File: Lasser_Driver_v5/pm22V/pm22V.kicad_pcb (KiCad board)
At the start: 2 copper layers, 160 x 100 mm, 26 parts, among them J5 Screw_Terminal_01x03, J6 DIN41612_M_3x8+8_Power_Male, Q1 IRF540NPBF, Q2 IRF9540NPBF

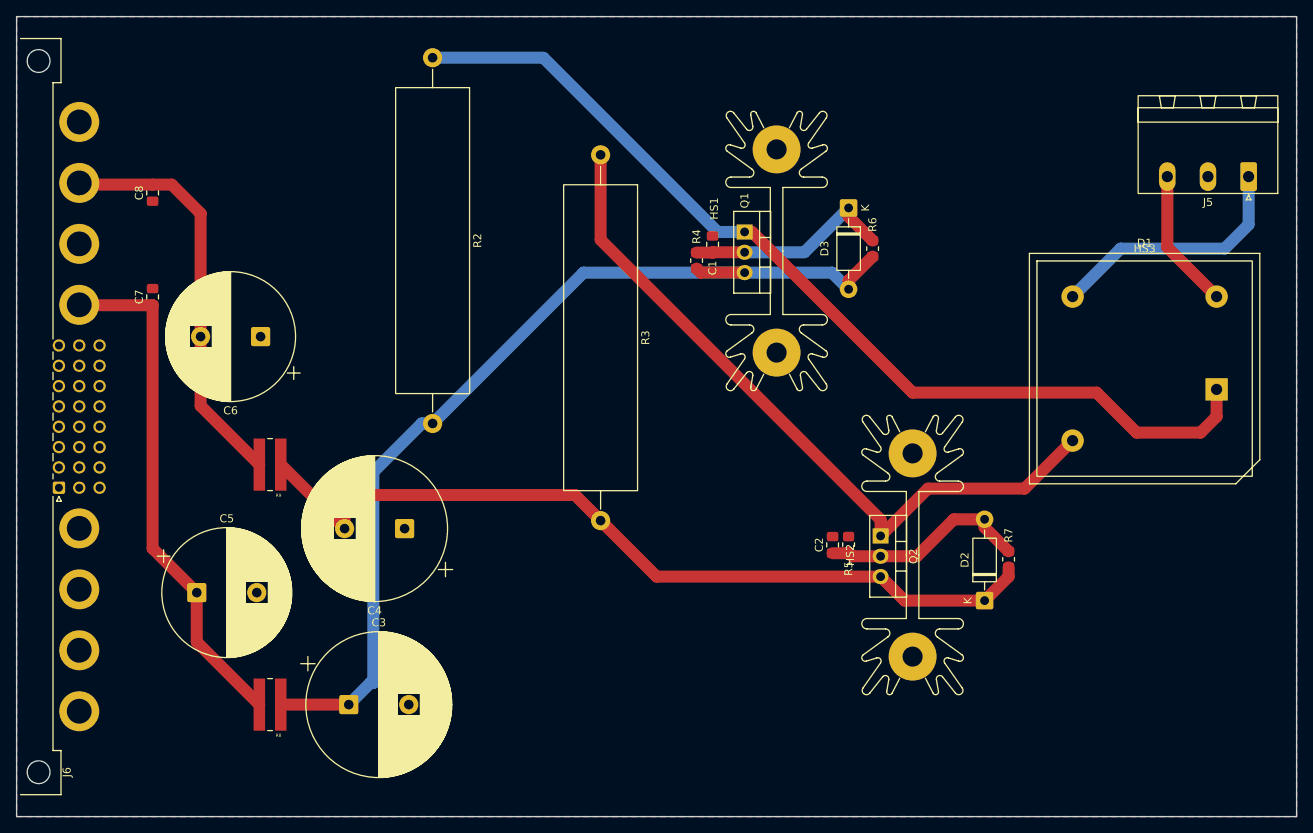
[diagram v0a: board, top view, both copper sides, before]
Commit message: v5 ac board and pm22V board ready
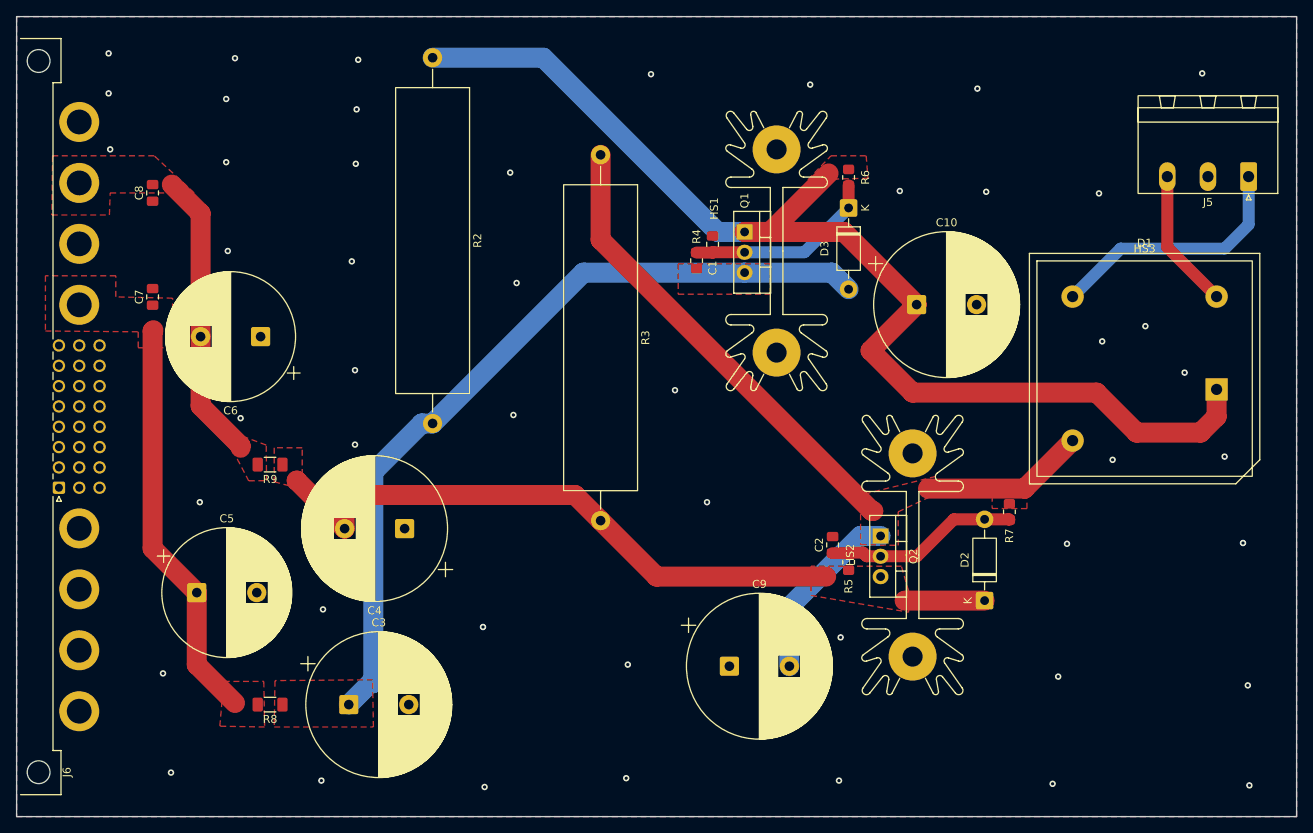
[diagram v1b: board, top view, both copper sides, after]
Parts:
- added C10: 2200uF 50V, Capacitor_THT:CP_Radial_D18.0mm_P7.50mm, F.Cu at (167.5, 81.0)
- added C9: 2200uF 50V, Capacitor_THT:CP_Radial_D18.0mm_P7.50mm, F.Cu at (144.1, 126.2)
- R8: value 4.75 2W -> 0.47; footprint RCL12254R75FKEG:RESC3263X80N -> Resistor_SMD:R_1206_3216Metric_Pad1.30x1.75mm_HandSolder
- R9: value 4.75, 2+W -> 0.47; footprint RCL12254R75FKEG:RESC3263X80N -> Resistor_SMD:R_1206_3216Metric_Pad1.30x1.75mm_HandSolder
- moved R6 9.39 mm to (159.0, 65.1), turned to -90 degrees
- moved R7 5.94 mm to (179.1, 106.9), turned to -90 degrees
- moved R5 2.20 mm to (159.0, 113.2)
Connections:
- net +22V renamed +18V
- net +22Vac renamed +18Vac
- net -22V renamed -18V
- net -22Vac renamed -18Vac
- C3 pad 1: /+22VNF -> /+18VNF
- C4 pad 2: /-22VNF -> /-18VNF
- D2 pad 1: /-22VNF -> /-18VNF
- D3 pad 2: /+22VNF -> /+18VNF
- J5 pad 2: Net-(J5-Pin_2) -> GND
- J6 pad P6: Net-(J6-PadP6) -> GND
- J6 pad P8: Net-(J6-PadP8) -> GND
- Q1 pad 3: /+22VNF -> /+18VNF
- Q2 pad 3: /-22VNF -> /-18VNF
- R2 pad 2: /+22VNF -> /+18VNF
- R3 pad 2: /-22VNF -> /-18VNF
- R4 pad 2: /+22VNF -> /+18VNF
- R5 pad 1: Net-(D2-A) -> /-18VNF
- R5 pad 2: GND -> Net-(D2-A)
- R6 pad 1: /+22VNF -> /RAW22+
- R7 pad 1: /-22VNF -> /RAW22-
- R8 pad 1: /+22VNF -> /+18VNF
- R9 pad 1: /-22VNF -> /-18VNF
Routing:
- net /+22VNF: track 121.2 -> 0.00 mm
- net /-22VNF: track 105.2 -> 0.00 mm
- net /+18VNF: track 0.00 -> 101.2 mm
- net /-18VNF: track 0.00 -> 86.0 mm
- net /RAW22+: track 121.6 -> 146.7 mm
- net -18V: track 51.2 -> 36.8 mm
- net +18V: track 64.6 -> 51.0 mm
- net /RAW22-: track 91.1 -> 101.8 mm
- net Net-(D3-K): track 26.6 -> 24.1 mm
- net Net-(D2-A): track 26.4 -> 24.0 mm
- net GND: vias 0 -> 48
- added copper zone on F.Cu, net +18V
- added copper zone on F.Cu, net -18V
- added copper zone on F.Cu, net /+18VNF
- added copper zone on F.Cu, net /-18VNF
- added copper zone on F.Cu, net /RAW22+
- added copper zone on F.Cu, net /RAW22-
